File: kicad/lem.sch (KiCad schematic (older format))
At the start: 42 parts, among them J1501 tblock2x3, J1502 tblock2x3, J1503 tblock2x3, J1504 tblock2x3, J1505 tblock2x3, J1506 tblock2x3, U1501 LXS6-NPS, U1502 LXS6-NPS, U1503 LXS6-NPS, U1504 LXS6-NPS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

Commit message: I forgot that QUEP was diferential!! all to back....
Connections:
- net LemAU_1: now reaches J1503.1 (Pin_1), U1503.1 (IN1)
- net LemAU_2: now reaches J1503.2 (Pin_2), U1503.2 (IN2)
- net LemAU_3: now reaches J1503.3 (Pin_3), U1503.3 (IN3)
- net LemAU_4: now reaches J1503.4 (Pin_4), U1503.4 (OUT4)
- net LemAU_5: now reaches J1503.5 (Pin_5), U1503.5 (OUT5)
- net LemAU_6: now reaches J1503.6 (Pin_6), U1503.6 (OUT6)
- net LemBU_3: now reaches J1504.1 (Pin_1), U1504.3 (IN3)
- net LemBU_2: now reaches J1504.2 (Pin_2), U1504.2 (IN2)
- net LemBU_1: now reaches J1504.3 (Pin_3), U1504.1 (IN1)
- net LemBU_6: now reaches J1504.4 (Pin_4), U1504.6 (OUT6)
- net LemBU_5: now reaches J1504.5 (Pin_5), U1504.5 (OUT5)
- net LemBU_4: now reaches J1504.6 (Pin_6), U1504.4 (OUT4)
- net LemAV_1: now reaches J1501.1 (Pin_1), U1501.1 (IN1)
- net LemAV_2: now reaches J1501.2 (Pin_2), U1501.2 (IN2)
- net LemAV_3: now reaches J1501.3 (Pin_3), U1501.3 (IN3)
- net LemAV_4: now reaches J1501.4 (Pin_4), U1501.4 (OUT4)
- net LemAV_5: now reaches J1501.5 (Pin_5), U1501.5 (OUT5)
- net LemAV_6: now reaches J1501.6 (Pin_6), U1501.6 (OUT6)
- net LemA_All_1: now reaches J1502.1 (Pin_1), U1502.1 (IN1)
- net LemA_All_2: now reaches J1502.2 (Pin_2), U1502.2 (IN2)
- net LemA_All_3: now reaches J1502.3 (Pin_3), U1502.3 (IN3)
- net LemA_All_4: now reaches J1502.4 (Pin_4), U1502.4 (OUT4)
- net LemA_All_5: now reaches J1502.5 (Pin_5), U1502.5 (OUT5)
- net LemA_All_6: now reaches J1502.6 (Pin_6), U1502.6 (OUT6)
- net LemBV_3: now reaches J1505.1 (Pin_1), U1505.3 (IN3)
- net LemBV_2: now reaches J1505.2 (Pin_2), U1505.2 (IN2)
- net LemBV_1: now reaches J1505.3 (Pin_3), U1505.1 (IN1)
- net LemBV_6: now reaches J1505.4 (Pin_4), U1505.6 (OUT6)
- net LemBV_5: now reaches J1505.5 (Pin_5), U1505.5 (OUT5)
- net LemBV_4: now reaches J1505.6 (Pin_6), U1505.4 (OUT4)
- net LemB_All_1: now reaches J1506.3 (Pin_3), U1506.1 (IN1)
- net LemB_All_2: now reaches J1506.2 (Pin_2), U1506.2 (IN2)
- net LemB_All_3: now reaches J1506.1 (Pin_1), U1506.3 (IN3)
- net LemB_All_4: now reaches J1506.6 (Pin_6), U1506.4 (OUT4)
- net LemB_All_5: now reaches J1506.5 (Pin_5), U1506.5 (OUT5)
- net LemB_All_6: now reaches J1506.4 (Pin_4), U1506.6 (OUT6)
- no-connect marks 2 -> 1

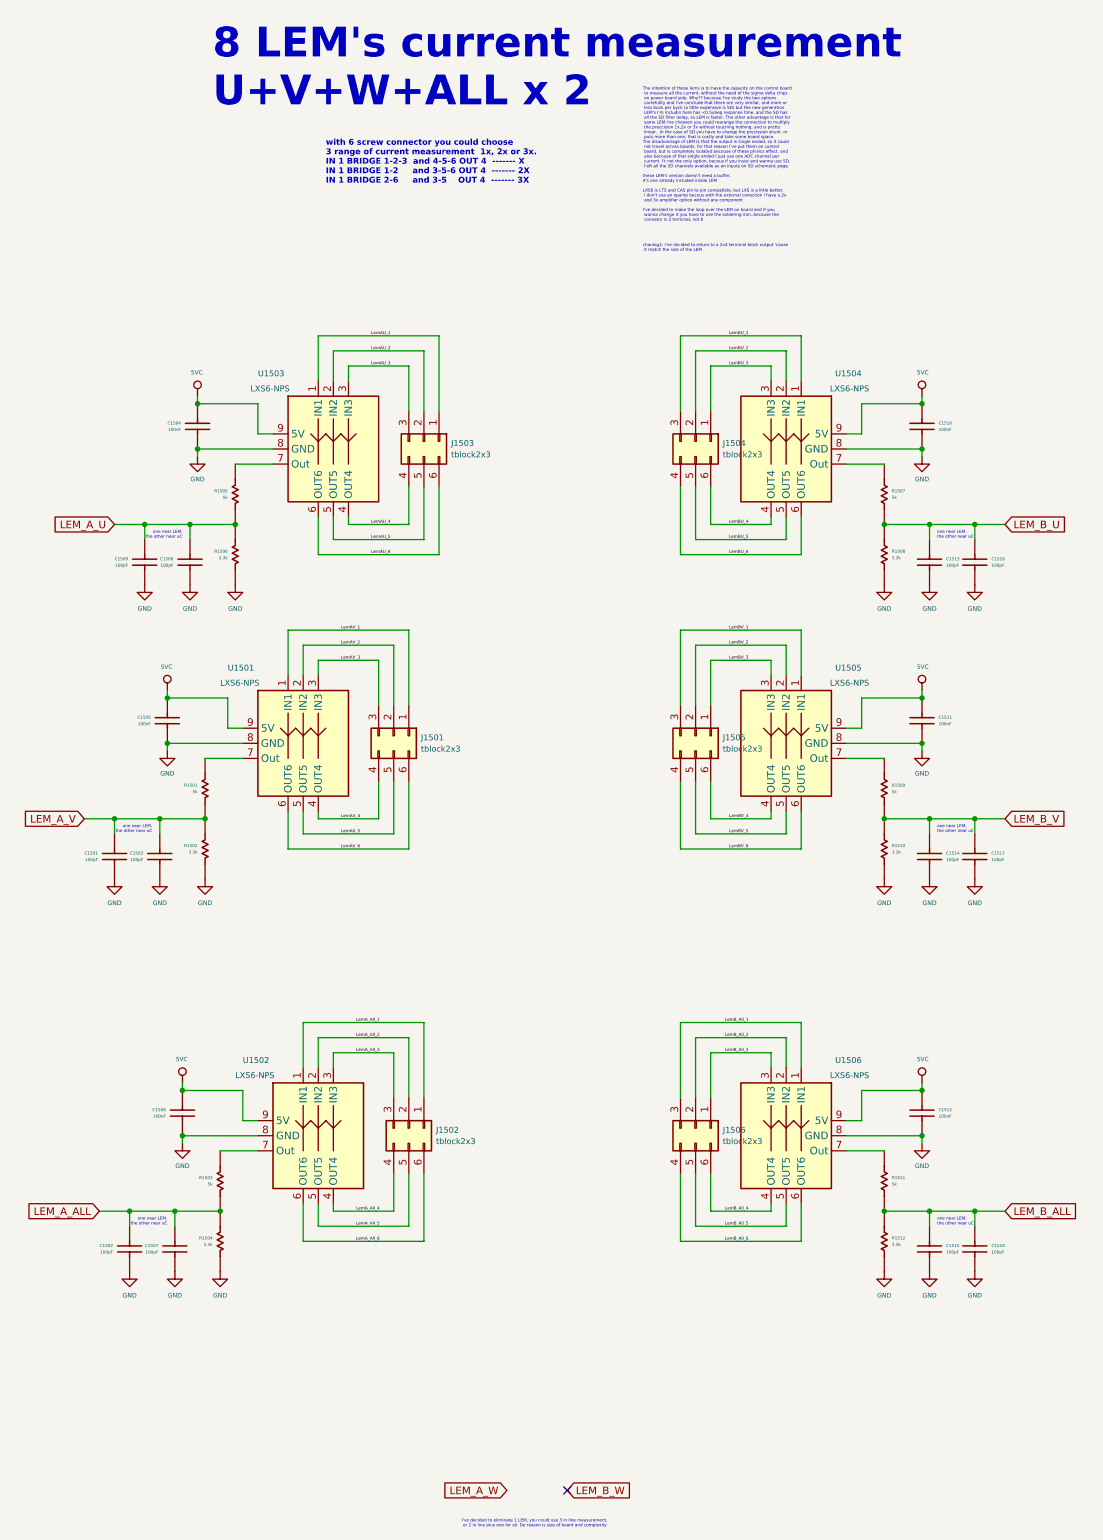
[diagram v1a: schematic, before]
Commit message: placing smmall capacitors and resistors nerar his group
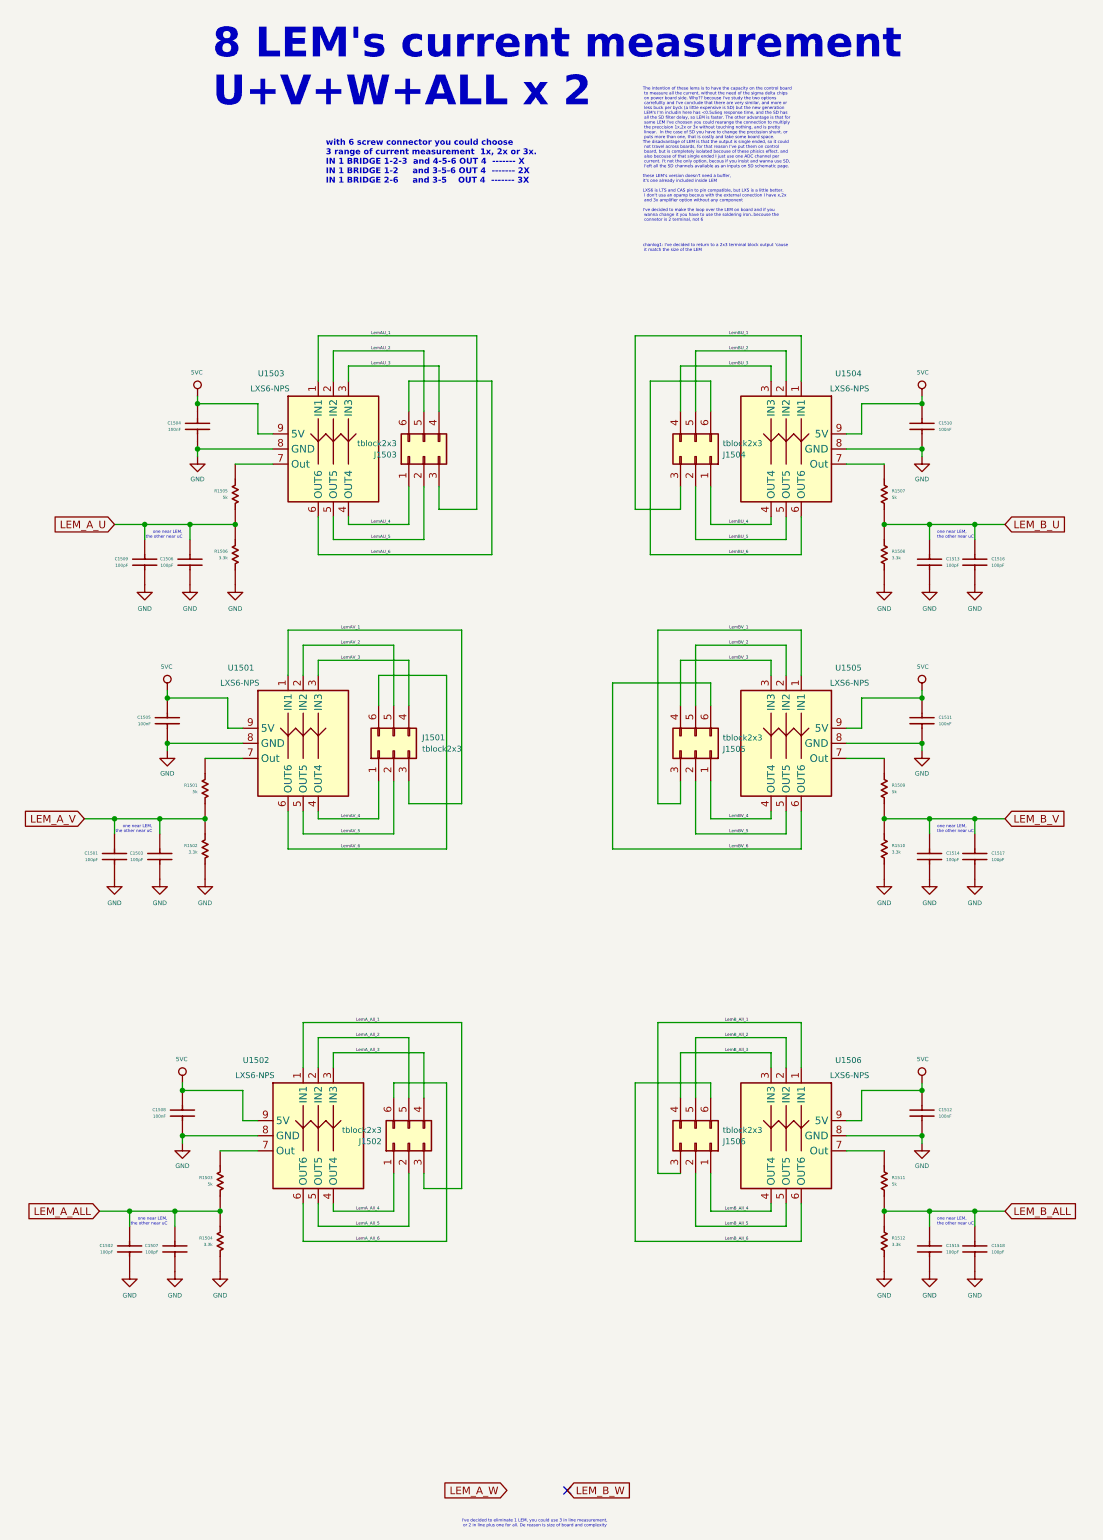
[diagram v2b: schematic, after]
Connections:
- net LemAU_1: now also J1503.3 (Pin_3); no longer J1503.1 (Pin_1)
- net LemAU_2: now also J1503.5 (Pin_5); no longer J1503.2 (Pin_2)
- net LemAU_3: now also J1503.4 (Pin_4); no longer J1503.3 (Pin_3)
- net LemAU_4: now also J1503.1 (Pin_1); no longer J1503.4 (Pin_4)
- net LemAU_5: now also J1503.2 (Pin_2); no longer J1503.5 (Pin_5)
- net LemAV_1: now also J1501.3 (Pin_3); no longer J1501.1 (Pin_1)
- net LemAV_2: now also J1501.5 (Pin_5); no longer J1501.2 (Pin_2)
- net LemAV_3: now also J1501.4 (Pin_4); no longer J1501.3 (Pin_3)
- net LemAV_4: now also J1501.1 (Pin_1); no longer J1501.4 (Pin_4)
- net LemAV_5: now also J1501.2 (Pin_2); no longer J1501.5 (Pin_5)
- net LemA_All_1: now also J1502.3 (Pin_3); no longer J1502.1 (Pin_1)
- net LemA_All_2: now also J1502.5 (Pin_5); no longer J1502.2 (Pin_2)
- net LemA_All_3: now also J1502.4 (Pin_4); no longer J1502.3 (Pin_3)
- net LemA_All_4: now also J1502.1 (Pin_1); no longer J1502.4 (Pin_4)
- net LemA_All_5: now also J1502.2 (Pin_2); no longer J1502.5 (Pin_5)
- net LemBU_2: now also J1504.5 (Pin_5); no longer J1504.2 (Pin_2)
- net LemBU_3: now also J1504.4 (Pin_4); no longer J1504.1 (Pin_1)
- net LemBU_4: now also J1504.1 (Pin_1); no longer J1504.6 (Pin_6)
- net LemBU_5: now also J1504.2 (Pin_2); no longer J1504.5 (Pin_5)
- net LemBU_6: now also J1504.6 (Pin_6); no longer J1504.4 (Pin_4)
- net LemBV_2: now also J1505.5 (Pin_5); no longer J1505.2 (Pin_2)
- net LemBV_3: now also J1505.4 (Pin_4); no longer J1505.1 (Pin_1)
- net LemBV_4: now also J1505.1 (Pin_1); no longer J1505.6 (Pin_6)
- net LemBV_5: now also J1505.2 (Pin_2); no longer J1505.5 (Pin_5)
- net LemBV_6: now also J1505.6 (Pin_6); no longer J1505.4 (Pin_4)
- net LemB_All_2: now also J1506.5 (Pin_5); no longer J1506.2 (Pin_2)
- net LemB_All_3: now also J1506.4 (Pin_4); no longer J1506.1 (Pin_1)
- net LemB_All_4: now also J1506.1 (Pin_1); no longer J1506.6 (Pin_6)
- net LemB_All_5: now also J1506.2 (Pin_2); no longer J1506.5 (Pin_5)
- net LemB_All_6: now also J1506.6 (Pin_6); no longer J1506.4 (Pin_4)
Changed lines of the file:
@@
 I've decided to eliminate 1 LEM, you could use 3 in line measurement,\n or 2 in line plus one for all. De reason is size of board and complexity
 Wire Wire Line
-	4750 2900 5550 2900
-Wire Wire Line
-	5550 2900 5550 3400
-Wire Wire Line
 	4850 3000 5450 3000
 Wire Wire Line
 	5450 3000 5450 3400
 Wire Wire Line
-	5350 3100 4950 3100
-Wire Wire Line
 	4750 2900 4750 3200
 Wire Wire Line
 	4850 3000 4850 3200
 Wire Wire Line
-	5350 3100 5350 3400
-Wire Wire Line
 	4950 4150 5350 4150
 Wire Wire Line
@@
 Wire Wire Line
 	5450 4250 5450 3900
-Wire Wire Line
-	5550 3900 5550 4350
-Wire Wire Line
-	5550 4350 4750 4350
 Wire Wire Line
 	4750 4100 4750 4350
@@
 L servo:tblock2x3 J1503
 U 1 1 5E261EDA
-P 5450 3600
-F 0 "J1503" V 5462 3780 39  0000 L CNN
-F 1 "tblock2x3" V 5537 3780 39  0000 L CNN
-F 2 "servo:tblock02x03" H 5400 3700 50  0001 C CNN
-F 3 "../doc/dfatasheets/tblock2rows.pdf" H 5500 3800 50  0001 C CNN
-	1    5450 3600
-	0    1    1    0
+P 5450 3700
+F 0 "J1503" V 5462 3880 39  0000 L CNN
+F 1 "tblock2x3" V 5537 3880 39  0000 L CNN
+F 2 "servo:tblock02x03" H 5400 3800 50  0001 C CNN
+F 3 "../doc/dfatasheets/tblock2rows.pdf" H 5500 3900 50  0001 C CNN
+	1    5450 3700
+	0    -1   -1   0
 $EndComp
 $Comp
 L servo:tblock2x3 J1504
 U 1 1 5E270F16
-P 7250 3600
-F 0 "J1504" V 7262 3780 39  0000 L CNN
-F 1 "tblock2x3" V 7337 3780 39  0000 L CNN
-F 2 "servo:tblock02x03" H 7200 3700 50  0001 C CNN
-F 3 "../doc/dfatasheets/tblock2rows.pdf" H 7300 3800 50  0001 C CNN
-	1    7250 3600
-	0    1    1    0
+P 7250 3700
+F 0 "J1504" V 7262 3880 39  0000 L CNN
+F 1 "tblock2x3" V 7337 3880 39  0000 L CNN
+F 2 "servo:tblock02x03" H 7200 3800 50  0001 C CNN
+F 3 "../doc/dfatasheets/tblock2rows.pdf" H 7300 3900 50  0001 C CNN
+	1    7250 3700
+	0    1    -1   0
 $EndComp
 $Comp
 L servo:tblock2x3 J1501
 U 1 1 5E2787AF
-P 5250 5550
-F 0 "J1501" V 5262 5730 39  0000 L CNN
-F 1 "tblock2x3" V 5337 5730 39  0000 L CNN
-F 2 "servo:tblock02x03" H 5200 5650 50  0001 C CNN
-F 3 "../doc/dfatasheets/tblock2rows.pdf" H 5300 5750 50  0001 C CNN
-	1    5250 5550
-	0    1    1    0
+P 5250 5650
+F 0 "J1501" V 5338 5462 39  0000 R CNN
+F 1 "tblock2x3" V 5263 5462 39  0000 R CNN
+F 2 "servo:tblock02x03" H 5200 5750 50  0001 C CNN
+F 3 "../doc/dfatasheets/tblock2rows.pdf" H 5300 5850 50  0001 C CNN
+	1    5250 5650
+	0    -1   -1   0
 $EndComp
 $Comp
 L servo:tblock2x3 J1505
 U 1 1 5E27FF32
-P 7250 5550
-F 0 "J1505" V 7262 5730 39  0000 L CNN
-F 1 "tblock2x3" V 7337 5730 39  0000 L CNN
-F 2 "servo:tblock02x03" H 7200 5650 50  0001 C CNN
-F 3 "../doc/dfatasheets/tblock2rows.pdf" H 7300 5750 50  0001 C CNN
-	1    7250 5550
-	0    1    1    0
+P 7250 5650
+F 0 "J1505" V 7262 5830 39  0000 L CNN
+F 1 "tblock2x3" V 7337 5830 39  0000 L CNN
+F 2 "servo:tblock02x03" H 7200 5750 50  0001 C CNN
+F 3 "../doc/dfatasheets/tblock2rows.pdf" H 7300 5850 50  0001 C CNN
+	1    7250 5650
+	0    1    -1   0
 $EndComp
 $Comp
 L servo:tblock2x3 J1502
 U 1 1 5E296823
-P 5350 8150
-F 0 "J1502" V 5362 8330 39  0000 L CNN
-F 1 "tblock2x3" V 5437 8330 39  0000 L CNN
-F 2 "servo:tblock02x03" H 5300 8250 50  0001 C CNN
-F 3 "../doc/dfatasheets/tblock2rows.pdf" H 5400 8350 50  0001 C CNN
-	1    5350 8150
-	0    1    1    0
+P 5350 8250
+F 0 "J1502" V 5362 8430 39  0000 L CNN
+F 1 "tblock2x3" V 5437 8430 39  0000 L CNN
+F 2 "servo:tblock02x03" H 5300 8350 50  0001 C CNN
+F 3 "../doc/dfatasheets/tblock2rows.pdf" H 5400 8450 50  0001 C CNN
+	1    5350 8250
+	0    -1   -1   0
 $EndComp
 $Comp
 L servo:tblock2x3 J1506
 U 1 1 5E29DFAC
-P 7250 8150
-F 0 "J1506" V 7262 8330 39  0000 L CNN
-F 1 "tblock2x3" V 7337 8330 39  0000 L CNN
-F 2 "servo:tblock02x03" H 7200 8250 50  0001 C CNN
-F 3 "../doc/datasheets/tblock2rows.pdf" H 7300 8350 50  0001 C CNN
-	1    7250 8150
-	0    1    1    0
+P 7250 8250
+F 0 "J1506" V 7262 8430 39  0000 L CNN
+F 1 "tblock2x3" V 7337 8430 39  0000 L CNN
+F 2 "servo:tblock02x03" H 7200 8350 50  0001 C CNN
+F 3 "../doc/datasheets/tblock2rows.pdf" H 7300 8450 50  0001 C CNN
+	1    7250 8250
+	0    1    -1   0
 $EndComp
 Text Label 5100 2900 0    20   ~ 0
@@
 	7950 7450 7950 7750
 Wire Wire Line
-	4550 4850 5350 4850
-Wire Wire Line
-	5350 4850 5350 5350
-Wire Wire Line
 	4650 4950 5250 4950
 Wire Wire Line
 	5250 4950 5250 5350
-Wire Wire Line
-	5150 5050 4750 5050
-Wire Wire Line
-	5150 5050 5150 5350
 Text Label 4900 4850 0    20   ~ 0
 LemAV_1
@@
 LemAV_3
 Wire Wire Line
-	4650 7450 5450 7450
-Wire Wire Line
-	5450 7450 5450 7950
-Wire Wire Line
 	4750 7550 5350 7550
 Wire Wire Line
 	5350 7550 5350 7950
-Wire Wire Line
-	5250 7650 4850 7650
-Wire Wire Line
-	5250 7650 5250 7950
 Text Label 5000 7450 0    20   ~ 0
 LemA_All_1
@@
 	4750 6100 5150 6100
 Wire Wire Line
-	5150 6100 5150 5850
-Wire Wire Line
 	4650 6200 5250 6200
 Wire Wire Line
 	5250 6200 5250 5850
-Wire Wire Line
-	5350 5850 5350 6300
-Wire Wire Line
-	5350 6300 4550 6300
 Text Label 4900 6100 0    20   ~ 0
 LemAV_4
@@
 Wire Wire Line
 	5350 8800 5350 8450
-Wire Wire Line
-	5450 8450 5450 8900
-Wire Wire Line
-	5450 8900 4650 8900
 Text Label 5000 8700 0    20   ~ 0
 LemA_All_4
@@
 LemA_All_6
 Wire Wire Line
-	7950 2900 7150 2900
-Wire Wire Line
-	7150 2900 7150 3400
-Wire Wire Line
 	7850 3000 7250 3000
 Wire Wire Line
 	7250 3000 7250 3400
 Wire Wire Line
-	7350 3100 7750 3100
-Wire Wire Line
-	7350 3100 7350 3400
-Wire Wire Line
 	7750 4150 7350 4150
 Wire Wire Line
-	7350 4150 7350 3900
-Wire Wire Line
 	7850 4250 7250 4250
 Wire Wire Line
 	7250 4250 7250 3900
-Wire Wire Line
-	7150 3900 7150 4350
-Wire Wire Line
-	7150 4350 7950 4350
 Text Label 7600 2900 2    20   ~ 0
 LemBU_1
@@
 LemBU_6
 Wire Wire Line
-	7950 4850 7150 4850
-Wire Wire Line
-	7150 4850 7150 5350
-Wire Wire Line
 	7850 4950 7250 4950
 Wire Wire Line
 	7250 4950 7250 5350
 Wire Wire Line
-	7350 5050 7750 5050
-Wire Wire Line
-	7350 5050 7350 5350
-Wire Wire Line
-	7750 6100 7350 6100
-Wire Wire Line
-	7350 6100 7350 5850
-Wire Wire Line
 	7850 6200 7250 6200
 Wire Wire Line
 	7250 6200 7250 5850
-Wire Wire Line
-	7150 5850 7150 6300
-Wire Wire Line
-	7150 6300 7950 6300
 Text Label 7600 4850 2    20   ~ 0
 LemBV_1
@@
 LemBV_6
 Wire Wire Line
-	7950 7450 7150 7450
-Wire Wire Line
-	7150 7450 7150 7950
-Wire Wire Line
 	7850 7550 7250 7550
 Wire Wire Line
-	7250 7550 7250 7950
-Wire Wire Line
-	7350 7650 7750 7650
-Wire Wire Line
-	7350 7650 7350 7950
-Wire Wire Line
 	7750 8700 7350 8700
 Wire Wire Line
@@
 Wire Wire Line
 	7250 8800 7250 8450
-Wire Wire Line
-	7150 8450 7150 8900
-Wire Wire Line
-	7150 8900 7950 8900
 Text Label 7600 7450 2    20   ~ 0
 LemB_All_1
@@
 Text Label 7600 8900 2    20   ~ 0
 LemB_All_6
+Wire Wire Line
+	7250 7550 7250 7950
+Wire Wire Line
+	7150 8450 7000 8450
+Wire Wire Line
+	7000 8450 7000 7450
+Wire Wire Line
+	7000 7450 7950 7450
+Wire Wire Line
+	7150 7650 7150 7950
+Wire Wire Line
+	7150 7650 7750 7650
+Wire Wire Line
+	7350 7850 7350 7950
+Wire Wire Line
+	7350 7850 6850 7850
+Wire Wire Line
+	6850 7850 6850 8900
+Wire Wire Line
+	6850 8900 7950 8900
+Wire Wire Line
+	5600 8900 5600 7850
+Wire Wire Line
+	5600 7850 5250 7850
+Wire Wire Line
+	4650 8900 5600 8900
+Wire Wire Line
+	5700 8550 5450 8550
+Wire Wire Line
+	5450 8550 5450 8450
+Wire Wire Line
+	4850 7650 5450 7650
+Wire Wire Line
+	5600 6300 5600 5150
+Wire Wire Line
+	5600 5150 5150 5150
+Wire Wire Line
+	5150 5150 5150 5350
+Wire Wire Line
+	4550 6300 5600 6300
+Wire Wire Line
+	4750 5050 5350 5050
+Wire Wire Line
+	5700 4850 5700 6000
+Wire Wire Line
+	5700 6000 5350 6000
+Wire Wire Line
+	5350 6000 5350 5850
+Wire Wire Line
+	4550 4850 5700 4850
+Wire Wire Line
+	5350 5050 5350 5350
+Wire Wire Line
+	5150 6100 5150 5850
+Wire Wire Line
+	5800 4050 5550 4050
+Wire Wire Line
+	5550 4050 5550 3900
+Wire Wire Line
+	4950 3100 5550 3100
+Wire Wire Line
+	5900 4350 5900 3200
+Wire Wire Line
+	5900 3200 5350 3200
+Wire Wire Line
+	5350 3200 5350 3400
+Wire Wire Line
+	4750 4350 5900 4350
+Wire Wire Line
+	5250 7850 5250 7950
+Wire Wire Line
+	5450 7650 5450 7950
+Wire Wire Line
+	5700 7450 5700 8550
+Wire Wire Line
+	4650 7450 5700 7450
+Wire Wire Line
+	5550 3100 5550 3400
+Wire Wire Line
+	5800 2900 5800 4050
+Wire Wire Line
+	4750 2900 5800 2900
+Wire Wire Line
+	7000 4850 7950 4850
+Wire Wire Line
+	6700 6300 6700 5200
+Wire Wire Line
+	6700 5200 7350 5200
+Wire Wire Line
+	7350 5200 7350 5350
+Wire Wire Line
+	6700 6300 7950 6300
+Wire Wire Line
+	7000 4850 7000 6000
+Wire Wire Line
+	7150 5050 7750 5050
+Wire Wire Line
+	7150 5050 7150 5350
+Wire Wire Line
+	7350 5850 7350 6100
+Wire Wire Line
+	7350 6100 7750 6100
+Wire Wire Line
+	7000 6000 7150 6000
+Wire Wire Line
+	7150 6000 7150 5850
+Wire Wire Line
+	6850 2900 6850 4050
+Wire Wire Line
+	6850 2900 7950 2900
+Wire Wire Line
+	6850 4050 7150 4050
+Wire Wire Line
+	7150 4050 7150 3900
+Wire Wire Line
+	6950 4350 6950 3200
+Wire Wire Line
+	6950 4350 7950 4350
+Wire Wire Line
+	7350 4150 7350 3900
+Wire Wire Line
+	7350 3200 7350 3400
+Wire Wire Line
+	6950 3200 7350 3200
+Wire Wire Line
+	7150 3100 7750 3100
+Wire Wire Line
+	7150 3100 7150 3400
 $EndSCHEMATC
